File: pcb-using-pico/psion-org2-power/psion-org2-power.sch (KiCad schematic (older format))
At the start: 51 parts, among them J1 Conn_02x08_Odd_Even, J2 Conn_02x08_Odd_Even, J3 Conn_01x27_Female, J4 Conn_02x08_Odd_Even, J5 Conn_01x11_Female, J6 Conn_01x02_Female, M1 P-CHANNEL-MOSFET, M2 P-CHANNEL-MOSFET, M3 AO3401, U1 ESP32-WROOM-32, U2 AMS1117-3.3, U3 CAT24C256, U4 CAT24C256, U5 74HC595, U6 74LS245, U7 74LS245, U8 Regulator_Switching_MT3608

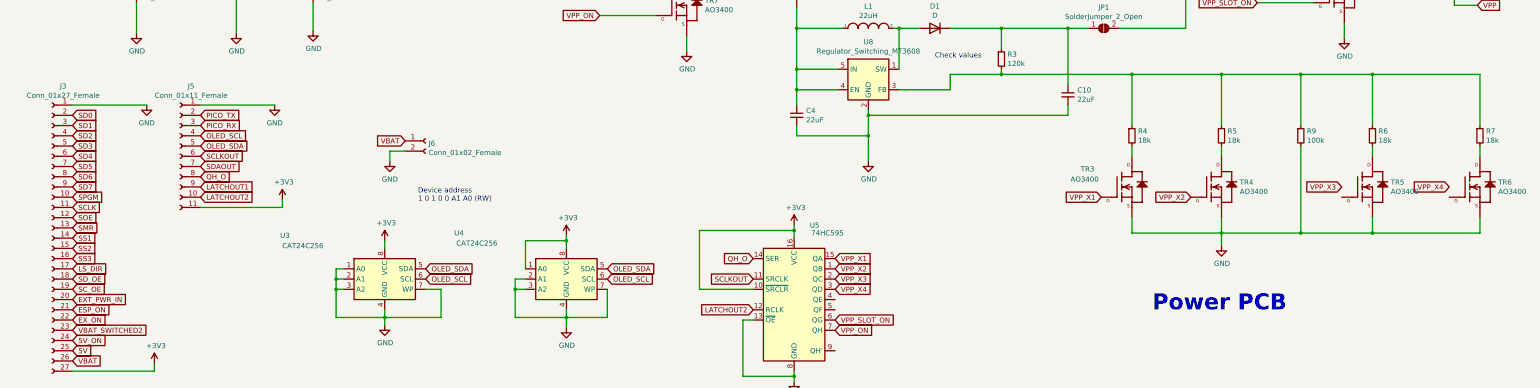
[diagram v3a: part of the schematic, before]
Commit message: First main PCB layout
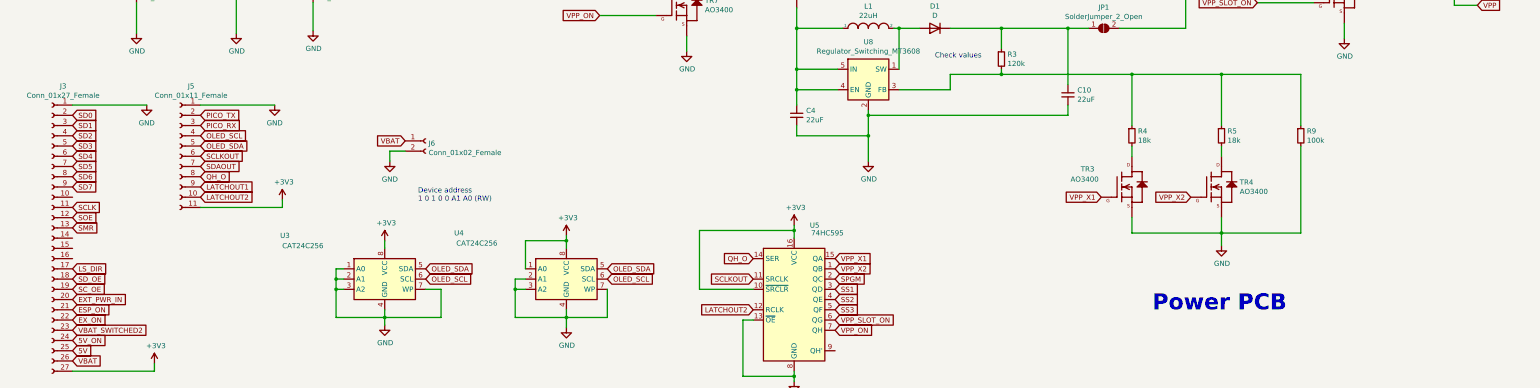
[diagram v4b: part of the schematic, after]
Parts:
- removed R6, R7: 18k, Resistor_SMD:R_0805_2012Metric_Pad1.15x1.40mm_HandSolder, symbol Device:R_Small
- removed TR5, TR6: AO3400, Package_TO_SOT_SMD:SOT-23, symbol New_Library:Si2302CDS-n-channel
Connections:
- net VPP_X3 is gone; now on net SPGM: U5.2 (QC)
- net VPP_X4 is gone; now on net SS1: U5.3 (QD)
- net SPGM: no longer J3.10 (Pin_10)
- net SS1: no longer J3.14 (Pin_14)
- net SS2: now also U5.4 (QE); no longer J3.15 (Pin_15)
- net SS3: now also U5.5 (QF); no longer J3.16 (Pin_16)
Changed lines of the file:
@@
 Text GLabel 1350 9350 2    50   Input ~ 0
 SOE
-Text GLabel 1350 9150 2    50   Input ~ 0
-SPGM
-Text GLabel 1350 9550 2    50   Input ~ 0
-SS1
 Text GLabel 1350 9250 2    50   Input ~ 0
 SCLK
@@
 	1    0    0    -1
 $EndComp
-Text GLabel 1350 9650 2    50   Input ~ 0
-SS2
-Text GLabel 1350 9750 2    50   Input ~ 0
-SS3
 Text GLabel 8425 2025 0    50   Input ~ 0
 SS2
@@
 Text GLabel 8800 9850 2    50   Input ~ 0
 VPP_X2
-Text GLabel 8800 9950 2    50   Input ~ 0
-VPP_X3
-Text GLabel 8800 10050 2    50   Input ~ 0
-VPP_X4
 Wire Wire Line
 	9925 8100 9925 7950
@@
 $EndComp
 $Comp
-L New_Library:Si2302CDS-n-channel TR5
-U 1 1 61AB7A55
-P 13950 9050
-F 0 "TR5" H 14228 9096 50  0000 L CNN
-F 1 "AO3400" H 14228 9005 50  0000 L CNN
-F 2 "Package_TO_SOT_SMD:SOT-23" H 13980 9200 20  0001 C CNN
-F 3 "" H 13950 9050 50  0001 C CNN
-	1    13950 9050
-	1    0    0    -1
-$EndComp
-$Comp
 L Device:R_Small R?
 U 1 1 61AB89B8
@@
 	1    0    0    -1
 $EndComp
-$Comp
-L Device:R_Small R?
-U 1 1 61ABD6B4
-P 14050 8550
-AR Path="/6001B7D3/60296A19/61ABD6B4" Ref="R?"  Part="1"
-AR Path="/6001B7D3/61ABD6B4" Ref="R?"  Part="1"
-AR Path="/61535A67/61ABD6B4" Ref="R?"  Part="1"
-AR Path="/61A1673D/61ABD6B4" Ref="R?"  Part="1"
-AR Path="/61ABD6B4" Ref="R6"  Part="1"
-F 0 "R6" H 14109 8596 50  0000 L CNN
-F 1 "18k" H 14109 8505 50  0000 L CNN
-F 2 "Resistor_SMD:R_0805_2012Metric_Pad1.15x1.40mm_HandSolder" H 14050 8550 50  0001 C CNN
-F 3 "~" H 14050 8550 50  0001 C CNN
-	1    14050 8550
-	1    0    0    -1
-$EndComp
 Wire Wire Line
 	11700 8750 11700 8650
@@
 Wire Wire Line
 	11700 7950 10425 7950
-$Comp
-L New_Library:Si2302CDS-n-channel TR6
-U 1 1 61AD3932
-P 15000 9050
-F 0 "TR6" H 15278 9096 50  0000 L CNN
-F 1 "AO3400" H 15278 9005 50  0000 L CNN
-F 2 "Package_TO_SOT_SMD:SOT-23" H 15030 9200 20  0001 C CNN
-F 3 "" H 15000 9050 50  0001 C CNN
-	1    15000 9050
-	1    0    0    -1
-$EndComp
-$Comp
-L Device:R_Small R?
-U 1 1 61AD3938
-P 15100 8550
-AR Path="/6001B7D3/60296A19/61AD3938" Ref="R?"  Part="1"
-AR Path="/6001B7D3/61AD3938" Ref="R?"  Part="1"
-AR Path="/61535A67/61AD3938" Ref="R?"  Part="1"
-AR Path="/61A1673D/61AD3938" Ref="R?"  Part="1"
-AR Path="/61AD3938" Ref="R7"  Part="1"
-F 0 "R7" H 15159 8596 50  0000 L CNN
-F 1 "18k" H 15159 8505 50  0000 L CNN
-F 2 "Resistor_SMD:R_0805_2012Metric_Pad1.15x1.40mm_HandSolder" H 15100 8550 50  0001 C CNN
-F 3 "~" H 15100 8550 50  0001 C CNN
-	1    15100 8550
-	1    0    0    -1
-$EndComp
 Wire Wire Line
 	12575 7950 13350 7950
@@
 Wire Wire Line
 	12575 9500 13350 9500
-Wire Wire Line
-	14050 9500 14050 9350
 Connection ~ 12575 9500
-Wire Wire Line
-	14050 9500 15100 9500
-Wire Wire Line
-	15100 9500 15100 9350
-Connection ~ 14050 9500
 $Comp
 L power:GND #PWR0119
@@
 Text GLabel 12275 9150 0    50   Input ~ 0
 VPP_X2
-Text GLabel 13750 9050 0    50   Input ~ 0
-VPP_X3
-Text GLabel 14800 9050 0    50   Input ~ 0
-VPP_X4
 Text GLabel 4800 9950 2    50   Input ~ 0
 OLED_SCL
@@
 Wire Wire Line
 	13350 8450 13350 7950
-Connection ~ 13350 7950
 Wire Wire Line
 	13350 8650 13350 9500
-Connection ~ 13350 9500
-Wire Wire Line
-	13350 9500 14050 9500
-Wire Wire Line
-	13350 7950 14050 7950
-Wire Wire Line
-	14050 8750 14050 8650
-Wire Wire Line
-	14050 8450 14050 7950
-Connection ~ 14050 7950
-Wire Wire Line
-	14050 7950 15100 7950
-Wire Wire Line
-	15100 8450 15100 7950
-Wire Wire Line
-	15100 8650 15100 8750
 $Comp
 L New_Library:Si2302CDS-n-channel TR7
@@
 Wire Wire Line
 	4450 8700 4600 8700
+Text GLabel 8800 10050 2    50   Input ~ 0
+SS1
+Text GLabel 8800 10150 2    50   Input ~ 0
+SS2
+Text GLabel 8800 10250 2    50   Input ~ 0
+SS3
+Text GLabel 8800 9950 2    50   Input ~ 0
+SPGM
 $EndSCHEMATC

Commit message: First layouts for fabrication
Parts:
- removed C10, C4: 22uF, Capacitor_SMD:C_1210_3225Metric_Pad1.42x2.65mm_HandSolder, symbol Device:C_Small
- removed C11, C12, C9: 100n, Capacitor_SMD:C_0805_2012Metric, symbol Device:C
- removed C5: 1u, Capacitor_SMD:C_0805_2012Metric, symbol Device:C
- removed D1: D, Diode_SMD:D_SOD-123, symbol Device:D
- removed JP1: SolderJumper_2_Open, Jumper:SolderJumper-2_P1.3mm_Open_RoundedPad1.0x1.5mm, symbol Jumper:SolderJumper_2_Open
- removed L1: 22uH, Inductor_SMD:L_Coilcraft_LPS5030, symbol pspice:INDUCTOR
- removed M2: P-CHANNEL-MOSFET, Package_TO_SOT_SMD:SOT-23, symbol GeekAmmo:P-CHANNEL-MOSFET
- removed M3: AO3401, Package_TO_SOT_SMD:SOT-23, symbol GeekAmmo:P-CHANNEL-MOSFET
- removed R10: R_Small, Resistor_SMD:R_0805_2012Metric_Pad1.15x1.40mm_HandSolder, symbol Device:R_Small
- removed R3: 120k, Resistor_SMD:R_0805_2012Metric_Pad1.15x1.40mm_HandSolder, symbol Device:R_Small
- removed R4, R5: 18k, Resistor_SMD:R_0805_2012Metric_Pad1.15x1.40mm_HandSolder, symbol Device:R_Small
- removed R8, R9: 100k, Resistor_SMD:R_0805_2012Metric_Pad1.15x1.40mm_HandSolder, symbol Device:R_Small
- removed TR3, TR4, TR7, TR8: AO3400, Package_TO_SOT_SMD:SOT-23, symbol New_Library:Si2302CDS-n-channel
- removed U8: Regulator_Switching_MT3608, Package_TO_SOT_SMD:SOT-23-6, symbol cq1re1-cache:Regulator_Switching_MT3608
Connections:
- net P_SPGM: no longer J2.14 (Pin_14), J4.14 (Pin_14)
- net SPGM: no longer U5.2 (QC)
- net VPP: no longer names the net of J4.16 (Pin_16)
- net VPP: no longer J2.16 (Pin_16)
- net VPP_ON: no longer names the net of U5.7 (QH)
- net VPP_SLOT_ON: no longer names the net of U5.6 (QG)
- net VPP_X1: no longer names the net of U5.15 (QA)
- net VPP_X2: no longer names the net of U5.1 (QB)
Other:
- note removed: "Check values\n"

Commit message: Annotated ROM listin gupdate
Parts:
- added 10k, 10k?: R_Small, symbol Device:R_Small
- added C? (x3): 100n, Capacitor_SMD:C_0805_2012Metric, symbol Device:C
- added M?: P-CHANNEL-MOSFET, SOT23-3, symbol GeekAmmo:P-CHANNEL-MOSFET
- added TR?: Si2302CDS-n-channel, Package_TO_SOT_SMD:SOT-23, symbol New_Library:Si2302CDS-n-channel
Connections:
- net +3V3: now also C?.1, C?.1, C?.1
- net ESP_ON: now also TR?.1 (G)
- net GND: now also C3.2, U1.1 (GND), U1.15 (GND), U1.38 (GND), U1.39 (GND), C?.2, C?.2, C?.2, TR?.2 (S); no longer TR2.2 (S)
- net SPGM: now also J2.14 (Pin_14), J3.10 (Pin_10), J4.14 (Pin_14)
- net VBAT_SWITCHED2: now also 10k.1, M?.2 (S); no longer C1.1, U2.3 (VI)
- new net: 10k.2, 10k?.1, M?.1 (G)
- new net: 10k?.2, TR?.3 (D)
- new net ESP_IN_POWER: C1.1, M?.3 (D), U2.3 (VI)
- now unconnected: TR2.3 (D)
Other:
- note added: "A030?\n"
- moved on the sheet: TR2
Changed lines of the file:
@@
 Title "Psion Organiser 2 Re-Creation"
 Date "2021-11-08"
-Rev "REV1"
+Rev "REV1.1"
 Comp ""
 Comment1 ""
@@
 	1    0    0    -1
 $EndComp
-$Comp
-L New_Library:Si2302CDS-n-channel TR2
-U 1 1 61990652
-P 13900 4675
-F 0 "TR2" H 14178 4721 50  0000 L CNN
-F 1 "Si2302CDS-n-channel" H 14178 4630 50  0000 L CNN
-F 2 "Package_TO_SOT_SMD:SOT-23" H 13930 4825 20  0001 C CNN
-F 3 "" H 13900 4675 50  0001 C CNN
-	1    13900 4675
-	1    0    0    -1
-$EndComp
 Wire Wire Line
 	14000 4100 14000 4250
 Connection ~ 14000 4250
-Wire Wire Line
-	14000 4250 14000 4375
-Wire Wire Line
-	14000 4975 14000 5150
-Text GLabel 13175 4775 0    50   Input ~ 0
-ESP_ON
-Wire Wire Line
-	13175 4775 13700 4775
 $Comp
 L pak_breakout:AMS1117-3.3 U2
@@
 	1    0    0    -1
 $EndComp
-Text GLabel 1500 6825 0    50   Input ~ 0
+Text GLabel 1500 6025 0    50   Input ~ 0
 VBAT_SWITCHED2
 Text GLabel 4025 6825 2    50   Input ~ 0
@@
 Text GLabel 8800 10250 2    50   Input ~ 0
 SS3
+$Comp
+L GeekAmmo:P-CHANNEL-MOSFET M?
+U 1 1 61B597B3
+P 14800 6775
+F 0 "M?" H 15078 6821 50  0000 L CNN
+F 1 "P-CHANNEL-MOSFET" H 15078 6730 50  0000 L CNN
+F 2 "SOT23-3" H 14830 6925 20  0001 C CNN
+F 3 "" H 14800 6775 50  0001 C CNN
+	1    14800 6775
+	1    0    0    -1
+$EndComp
+$Comp
+L New_Library:Si2302CDS-n-channel TR?
+U 1 1 61B5C6C5
+P 13500 7175
+F 0 "TR?" H 13778 7221 50  0000 L CNN
+F 1 "Si2302CDS-n-channel" H 13778 7130 50  0000 L CNN
+F 2 "Package_TO_SOT_SMD:SOT-23" H 13530 7325 20  0001 C CNN
+F 3 "" H 13500 7175 50  0001 C CNN
+	1    13500 7175
+	1    0    0    -1
+$EndComp
+Text GLabel 12775 7275 0    50   Input ~ 0
+ESP_ON
+Wire Wire Line
+	12775 7275 13300 7275
+$Comp
+L power:GND #PWR?
+U 1 1 61B61074
+P 13600 7650
+F 0 "#PWR?" H 13600 7400 50  0001 C CNN
+F 1 "GND" H 13605 7477 50  0000 C CNN
+F 2 "" H 13600 7650 50  0001 C CNN
+F 3 "" H 13600 7650 50  0001 C CNN
+	1    13600 7650
+	1    0    0    -1
+$EndComp
+Wire Wire Line
+	13600 7475 13600 7650
+Text GLabel 13225 5975 0    50   Input ~ 0
+VBAT_SWITCHED2
+Wire Wire Line
+	14900 5975 14900 6475
+$Comp
+L Device:R_Small 10k
+U 1 1 61B7C8DF
+P 13600 6150
+F 0 "10k" H 13659 6196 50  0000 L CNN
+F 1 "R_Small" H 13659 6105 50  0000 L CNN
+F 2 "" H 13600 6150 50  0001 C CNN
+F 3 "~" H 13600 6150 50  0001 C CNN
+	1    13600 6150
+	1    0    0    -1
+$EndComp
+Text GLabel 1500 6825 0    50   Input ~ 0
+ESP_IN_POWER
+Text GLabel 15125 7200 2    50   Input ~ 0
+ESP_IN_POWER
+Wire Wire Line
+	14900 7075 14900 7200
+Wire Wire Line
+	14900 7200 15125 7200
+Wire Wire Line
+	14075 5525 14600 5525
+Text GLabel 14075 5525 0    50   Input ~ 0
+ESP_ON
+$Comp
+L New_Library:Si2302CDS-n-channel TR2
+U 1 1 61990652
+P 14800 5425
+F 0 "TR2" H 15078 5471 50  0000 L CNN
+F 1 "Si2302CDS-n-channel" H 15078 5380 50  0000 L CNN
+F 2 "Package_TO_SOT_SMD:SOT-23" H 14830 5575 20  0001 C CNN
+F 3 "" H 14800 5425 50  0001 C CNN
+	1    14800 5425
+	1    0    0    -1
+$EndComp
+Wire Wire Line
+	14000 4250 14000 5150
+Wire Wire Line
+	13225 5975 13600 5975
+$Comp
+L Device:R_Small 10k?
+U 1 1 61BC3DC7
+P 13600 6475
+F 0 "10k?" H 13659 6521 50  0000 L CNN
+F 1 "R_Small" H 13659 6430 50  0000 L CNN
+F 2 "" H 13600 6475 50  0001 C CNN
+F 3 "~" H 13600 6475 50  0001 C CNN
+	1    13600 6475
+	1    0    0    -1
+$EndComp
+Wire Wire Line
+	13600 6575 13600 6875
+Wire Wire Line
+	13600 6375 13600 6300
+Wire Wire Line
+	13600 6050 13600 5975
+Connection ~ 13600 5975
+Wire Wire Line
+	13600 5975 14900 5975
+Wire Wire Line
+	13600 6300 14325 6300
+Wire Wire Line
+	14325 6300 14325 6675
+Wire Wire Line
+	14325 6675 14600 6675
+Connection ~ 13600 6300
+Wire Wire Line
+	13600 6300 13600 6250
+Text Notes 15350 6700 0    50   ~ 0
+A030?\n
+Text GLabel 1350 9150 2    50   Input ~ 0
+SPGM
+Text GLabel 11700 4225 2    50   Input ~ 0
+SPGM
+Text GLabel 11675 6125 2    50   Input ~ 0
+SPGM
+$Comp
+L power:+3V3 #PWR?
+U 1 1 61BE794A
+P 6575 7950
+F 0 "#PWR?" H 6575 7800 50  0001 C CNN
+F 1 "+3V3" H 6590 8123 50  0000 C CNN
+F 2 "" H 6575 7950 50  0001 C CNN
+F 3 "" H 6575 7950 50  0001 C CNN
+	1    6575 7950
+	1    0    0    -1
+$EndComp
+$Comp
+L Device:C C?
+U 1 1 61BE7950
+P 7100 8500
+F 0 "C?" H 7215 8546 50  0000 L CNN
+F 1 "100n" H 7215 8455 50  0000 L CNN
+F 2 "Capacitor_SMD:C_0805_2012Metric" H 7138 8350 50  0001 C CNN
+F 3 "~" H 7100 8500 50  0001 C CNN
+	1    7100 8500
+	1    0    0    -1
+$EndComp
+$Comp
+L Device:C C?
+U 1 1 61BE7956
+P 7550 8500
+F 0 "C?" H 7665 8546 50  0000 L CNN
+F 1 "100n" H 7665 8455 50  0000 L CNN
+F 2 "Capacitor_SMD:C_0805_2012Metric" H 7588 8350 50  0001 C CNN
+F 3 "~" H 7550 8500 50  0001 C CNN
+	1    7550 8500
+	1    0    0    -1
+$EndComp
+$Comp
+L Device:C C?
+U 1 1 61BE795C
+P 8000 8500
+F 0 "C?" H 8115 8546 50  0000 L CNN
+F 1 "100n" H 8115 8455 50  0000 L CNN
+F 2 "Capacitor_SMD:C_0805_2012Metric" H 8038 8350 50  0001 C CNN
+F 3 "~" H 8000 8500 50  0001 C CNN
+	1    8000 8500
+	1    0    0    -1
+$EndComp
+Wire Wire Line
+	8000 8350 8000 8300
+Wire Wire Line
+	7550 8350 7550 8300
+Connection ~ 7550 8300
+Wire Wire Line
+	7550 8300 8000 8300
+Wire Wire Line
+	7100 8350 7100 8300
+Wire Wire Line
+	7100 8300 7550 8300
+$Comp
+L power:GND #PWR?
+U 1 1 61BE7968
+P 8000 8800
+F 0 "#PWR?" H 8000 8550 50  0001 C CNN
+F 1 "GND" H 8005 8627 50  0000 C CNN
+F 2 "" H 8000 8800 50  0001 C CNN
+F 3 "" H 8000 8800 50  0001 C CNN
+	1    8000 8800
+	1    0    0    -1
+$EndComp
+Wire Wire Line
+	7100 8650 7100 8750
+Wire Wire Line
+	7550 8650 7550 8750
+Wire Wire Line
+	7550 8750 7100 8750
+Wire Wire Line
+	8000 8650 8000 8750
+$Comp
+L power:GND #PWR?
+U 1 1 61BE7972
+P 6575 8825
+F 0 "#PWR?" H 6575 8575 50  0001 C CNN
+F 1 "GND" H 6580 8652 50  0000 C CNN
+F 2 "" H 6575 8825 50  0001 C CNN
+F 3 "" H 6575 8825 50  0001 C CNN
+	1    6575 8825
+	1    0    0    -1
+$EndComp
+Wire Wire Line
+	7550 8750 8000 8750
+Connection ~ 7550 8750
+Connection ~ 8000 8750
+Wire Wire Line
+	8000 8750 8000 8800
+Wire Wire Line
+	6575 7950 6575 8300
+Wire Wire Line
+	7100 8300 6575 8300
+Connection ~ 7100 8300
+Wire Wire Line
+	7100 8750 6575 8750
+Connection ~ 7100 8750
+Wire Wire Line
+	6575 8750 6575 8825
 $EndSCHEMATC

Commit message: V1.1 started
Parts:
- added C12: 4u7, Capacitor_SMD:C_0805_2012Metric, symbol Device:C_Small
- added C4, C5: C_Small, Capacitor_SMD:C_0805_2012Metric, symbol Device:C_Small
- added D1: 3V0, Diode_SMD:D_SOD-123, symbol Device:D_Zener
- added D2: 4V7, Diode_SMD:D_SOD-123, symbol Device:D_Zener
- added J7: Conn_01x03_Female, Connector_PinHeader_2.54mm:PinHeader_1x03_P2.54mm_Vertical_SMD_Pin1Left, symbol Connector:Conn_01x03_Female
- added JP1: Jumper_NO_Small, Jumper:SolderJumper-2_P1.3mm_Open_RoundedPad1.0x1.5mm, symbol Device:Jumper_NO_Small
- added R10, R11, R12, R13, R14, R4, R5, R6, R7, R8, R9: 100k, Resistor_SMD:R_0805_2012Metric, symbol Device:R_Small
- added R3: R_Small, Resistor_SMD:R_0805_2012Metric, symbol Device:R_Small
- added U8: AMS1117-5.0, Package_TO_SOT_SMD:SOT-223-3_TabPin2, symbol pak_breakout:AMS1117-5.0
- C3: value C_Small -> 100nF
- M2: renamed from M?; footprint SOT23-3 -> Package_TO_SOT_SMD:SOT-23
- R16: renamed from 10k; value R_Small -> 10k; footprint (none) -> Resistor_SMD:R_0805_2012Metric
- R17: renamed from 10k?; value R_Small -> 10k; footprint (none) -> Resistor_SMD:R_0805_2012Metric
- TR2: value Si2302CDS-n-channel -> Si2302CDS-n-ch
- gave numbers to parts that had none: 4
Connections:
- net 5V: now also C5.1, U8.2 (VO)
- net ESP_ON: no longer TR2.1 (G)
- net EX_ON: now also TR2.1 (G), R12.2; no longer J3.22 (Pin_22)
- net GND: now also TR2.2 (S), C12.2, C4.2, C5.2, D1.2 (A), J7.2 (Pin_2), JP1.2, R10.2, R11.2, R14.2, R3.2, R4.2, R5.2, R6.2, R7.2, R8.2, R9.2, U8.1 (GND)
- net P_SD0: now also R11.1
- net P_SD1: now also R10.1
- net P_SD2: now also R9.1
- net P_SD3: now also R8.1
- net P_SD4: now also R7.1
- net P_SD5: now also R6.1
- net P_SD6: now also R5.1
- net P_SD7: now also R4.1
- net P_SPGM: now also J2.14 (Pin_14), J4.14 (Pin_14)
- net SPGM: no longer J2.14 (Pin_14), J4.14 (Pin_14)
- net VBAT: now also R13.1
- net VBAT_SWITCHED2: now also C4.1, D2.1 (K), U8.3 (VI)
- net at U6.9 (A7): now also R3.1
- net at U1.25 (IO0): now also JP1.1
- net at C3.1, R2.2, U1.3 (EN): now also C12.1
- net at U1.34 (RXD0/IO3): now also J7.3 (Pin_3)
- net at U1.35 (TXD0/IO1): now also J7.1 (Pin_1)
- net EX_ON_INV: now reaches TR2.3 (D)
- net EX_ON_INV: now also J3.22 (Pin_22), D1.1 (K), R12.1, R13.2, R14.1
- net at M2.1 (G), R16.2, R17.1: now also D2.2 (A)
- net BUZZER: now reaches J3.14 (Pin_14)
- net VBAT_SWITCHED1: now reaches J3.15 (Pin_15)
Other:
- note added: "*5V generated on this PCB*"
- moved on the sheet: C1, C2, R15, R16, R17, TR3, U2, U7
